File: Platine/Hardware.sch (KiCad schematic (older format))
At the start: 9 parts, among them U1 ESP32-WROOM-32, U2 ZLDO1117_SOT223, U3 TS2596S

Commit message: Spannungsregler hinzugfügt
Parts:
- added C3, C5: 470u, symbol Device:CP
- added C4, C6: 0,1u, symbol Device:C
- added D1: B340A, symbol Device:D_Zener
- added L1: 33u, symbol Device:L
- BT1: renamed from BT?; value Battery -> 9V
- U2: symbol Bauteile_DL7MLP:ZLDO1117_SOT223 -> Hardware-rescue:ZLDO1117_SOT223-Bauteile_DL7MLP
- U3: symbol Bauteile_DL7MLP:TS2596S -> Hardware-rescue:TS2596S-Bauteile_DL7MLP
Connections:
- wire segments 20 -> 50
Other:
- moved on the sheet: BT1

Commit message: Elkos ausgewählt
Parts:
- C3, C5: footprint (none) -> Capacitor_SMD:CP_Elec_6.3x7.7
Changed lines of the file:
@@
 F 0 "C3" H 6318 1146 50  0000 L CNN
 F 1 "470u" H 6318 1055 50  0000 L CNN
-F 2 "" H 6238 950 50  0001 C CNN
-F 3 "~" H 6200 1100 50  0001 C CNN
+F 2 "Capacitor_SMD:CP_Elec_6.3x7.7" H 6238 950 50  0001 C CNN
+F 3 "https://cdn-reichelt.de/documents/datenblatt/B300/SMD_FT_ENG_TDS.pdf" H 6200 1100 50  0001 C CNN
 	1    6200 1100
 	1    0    0    -1
@@
 F 0 "C5" H 8918 1146 50  0000 L CNN
 F 1 "470u" H 8918 1055 50  0000 L CNN
-F 2 "" H 8838 950 50  0001 C CNN
-F 3 "~" H 8800 1100 50  0001 C CNN
+F 2 "Capacitor_SMD:CP_Elec_6.3x7.7" H 8838 950 50  0001 C CNN
+F 3 "reichelt.de/documents/datenblatt/B300/SMD_FT_ENG_TDS.pdf" H 8800 1100 50  0001 C CNN
 	1    8800 1100
 	1    0    0    -1

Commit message: Erweiterung der Bauteilinformationen
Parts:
- removed D1: B340A, symbol Device:D_Zener
- added D1: B340A, symbol Device:D_Schottky
- C4, C6: footprint (none) -> Capacitor_SMD:C_0805_2012Metric_Pad1.18x1.45mm_HandSolder
- L1: footprint (none) -> Inductor_SMD:L_1008_2520Metric_Pad1.43x2.20mm_HandSolder
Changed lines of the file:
@@
 F 0 "C4" H 6615 1146 50  0000 L CNN
 F 1 "0,1u" H 6615 1055 50  0000 L CNN
-F 2 "" H 6538 950 50  0001 C CNN
-F 3 "~" H 6500 1100 50  0001 C CNN
+F 2 "Capacitor_SMD:C_0805_2012Metric_Pad1.18x1.45mm_HandSolder" H 6538 950 50  0001 C CNN
+F 3 "https://cdn-reichelt.de/documents/datenblatt/B300/KEM_C0XXX_C0G_DB-EN.pdf" H 6500 1100 50  0001 C CNN
 	1    6500 1100
 	1    0    0    -1
@@
 F 0 "L1" V 8590 950 50  0000 C CNN
 F 1 "33u" V 8499 950 50  0000 C CNN
-F 2 "" H 8400 950 50  0001 C CNN
-F 3 "~" H 8400 950 50  0001 C CNN
+F 2 "Inductor_SMD:L_1008_2520Metric_Pad1.43x2.20mm_HandSolder" H 8400 950 50  0001 C CNN
+F 3 "https://cdn-reichelt.de/documents/datenblatt/B400/1008F.pdf" H 8400 950 50  0001 C CNN
 	1    8400 950
 	0    -1   -1   0
@@
 F 0 "C6" H 9215 1146 50  0000 L CNN
 F 1 "0,1u" H 9215 1055 50  0000 L CNN
-F 2 "" H 9138 950 50  0001 C CNN
-F 3 "~" H 9100 1100 50  0001 C CNN
+F 2 "Capacitor_SMD:C_0805_2012Metric_Pad1.18x1.45mm_HandSolder" H 9138 950 50  0001 C CNN
+F 3 "https://cdn-reichelt.de/documents/datenblatt/B300/KEM_C0XXX_C0G_DB-EN.pdf" H 9100 1100 50  0001 C CNN
 	1    9100 1100
 	1    0    0    -1
@@
 $EndComp
 $Comp
-L Device:D_Zener D1
-U 1 1 5FB55D4C
-P 8200 1250
-F 0 "D1" V 8154 1330 50  0000 L CNN
-F 1 "B340A" V 8245 1330 50  0000 L CNN
-F 2 "" H 8200 1250 50  0001 C CNN
-F 3 "~" H 8200 1250 50  0001 C CNN
-	1    8200 1250
-	0    1    1    0
-$EndComp
-$Comp
 L power:GND #PWR?
 U 1 1 5FB57356
@@
 Wire Notes Line
 	5450 650  5450 1650
+$Comp
+L Device:D_Schottky D1
+U 1 1 5FB4F340
+P 8200 1250
+F 0 "D1" V 8154 1330 50  0000 L CNN
+F 1 "B340A" V 8245 1330 50  0000 L CNN
+F 2 "" H 8200 1250 50  0001 C CNN
+F 3 "~" H 8200 1250 50  0001 C CNN
+	1    8200 1250
+	0    1    1    0
+$EndComp
 $EndSCHEMATC

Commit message: Finished LED Matrix Added part datasheets Updated BOM
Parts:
- removed C? (x2): C, symbol Device:C
- removed U1: ESP32-WROOM-32, RF_Module:ESP32-WROOM-32, symbol RF_Module:ESP32-WROOM-32
- added C?: 100n, Resistor_SMD:R_0805_2012Metric_Pad1.15x1.40mm_HandSolder, symbol Device:C
- added C? (x41): 100n, symbol Device:C
- added D? (x41): WS2812S, LED_SMD:LED_WS2812_PLCC6_5.0x5.0mm_P1.6mm, symbol LED:WS2812S
- added R? (x42): 91, Resistor_SMD:R_0805_2012Metric_Pad1.15x1.40mm_HandSolder, symbol Device:R
- added U1: ESP32-WROOM-32D, RF_Module:ESP32-WROOM-32, symbol RF_Module:ESP32-WROOM-32D
- D1: footprint (none) -> Diode_SMD:D_SMA_Handsoldering
- L1: footprint Inductor_SMD:L_1008_2520Metric_Pad1.43x2.20mm_HandSolder -> Footprints_DL7MLP:L_1008_2520Metric_Pad1.43x2.20mm_HandSolder
- U2: symbol Hardware-rescue:ZLDO1117_SOT223-Bauteile_DL7MLP -> Bauteile_DL7MLP:ZLDO1117_SOT223
- U3: symbol Hardware-rescue:TS2596S-Bauteile_DL7MLP -> Bauteile_DL7MLP:TS2596S
- gave numbers to parts that had none: 1
- renumbered D1 to D2
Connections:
- wire segments 50 -> 556
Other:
- note added: "Led Matrix\nSpielfeld"
- note added: "Regulator 3V3"
- note added: "Regulator 5V"
- moved on the sheet: BT1, C1, C2, C3, C4, C5, C6, D1, D2, L1

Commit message: LED-Matrix Baueilnummerierung hinzugefügt und BOM erweitert
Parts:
- C10, C11, C12, C13, C14, C15, C16, C17, C18, C19, C20, C21, C22, C23, C24, C25, C26, C27, C28, C29, C30, C31, C32, C33, C34, C35, C36, C37, C38, C39, C40, C41, C42, C43, C44, C45, C46, C47, C48, C8, C9: renamed from C?; footprint (none) -> Resistor_SMD:R_0805_2012Metric_Pad1.15x1.40mm_HandSolder
- L1: footprint Footprints_DL7MLP:L_1008_2520Metric_Pad1.43x2.20mm_HandSolder -> Custom_Footprints:L_1008_2520Metric_Pad1.43x2.20mm_HandSolder
- U2: symbol Bauteile_DL7MLP:ZLDO1117_SOT223 -> Custom_Symbols:ZLDO1117_SOT223
- U3: symbol Bauteile_DL7MLP:TS2596S -> Custom_Symbols:TS2596S
- gave numbers to parts that had none: 84

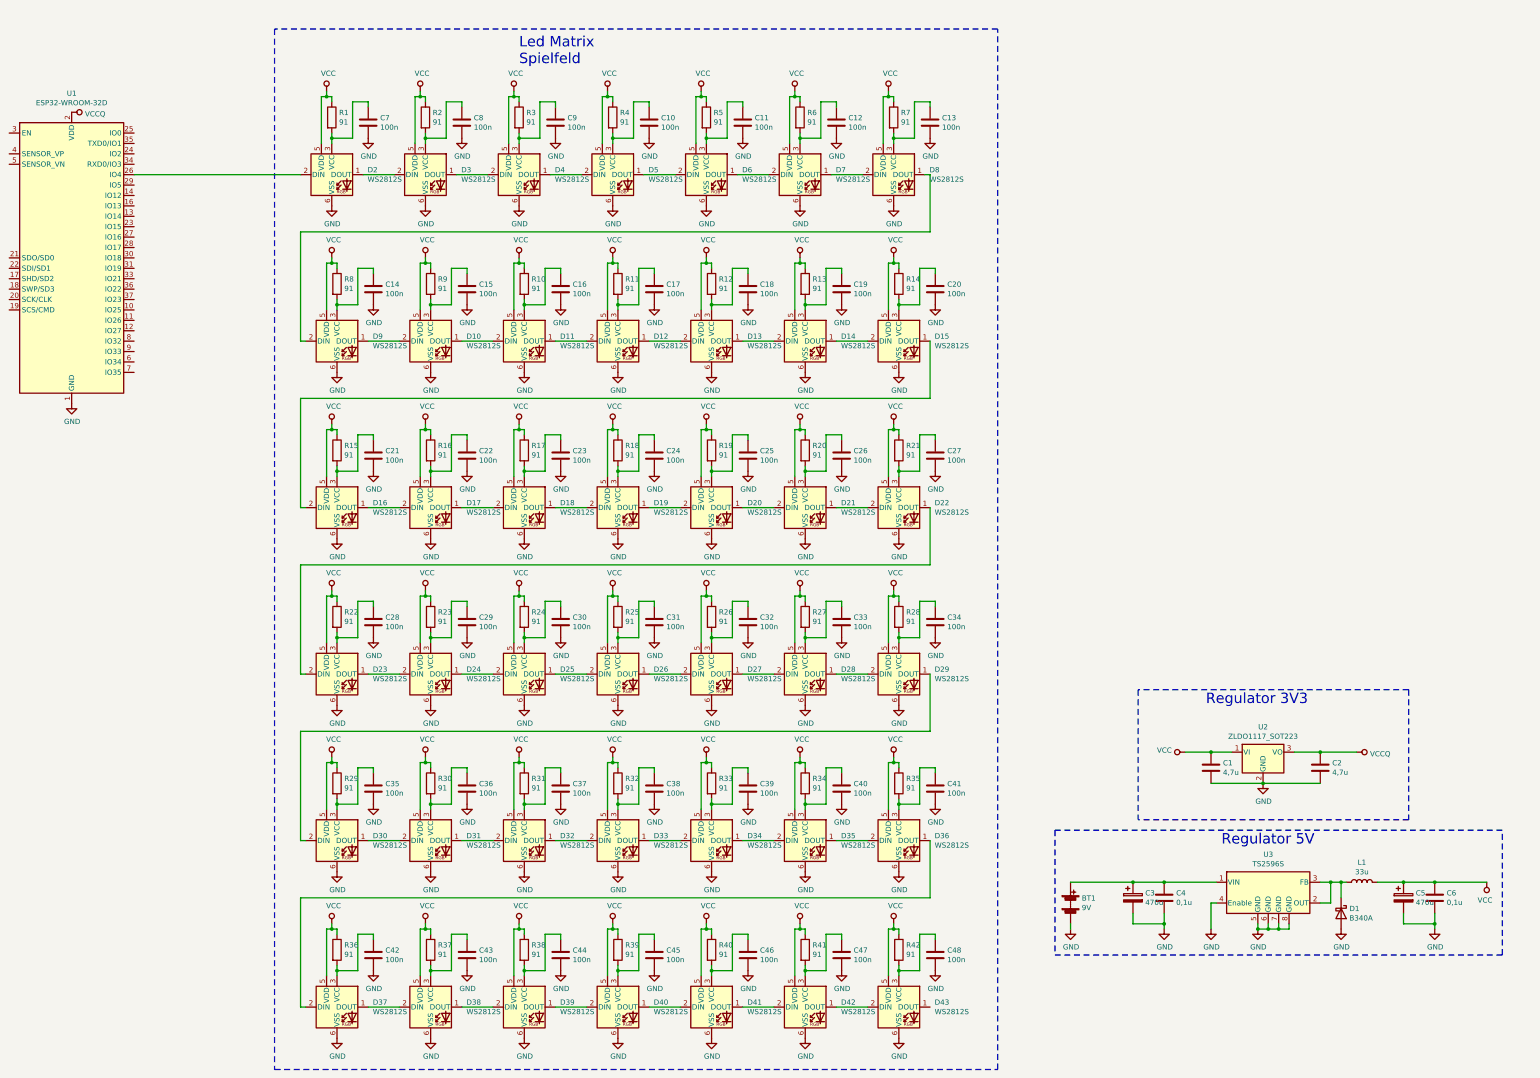
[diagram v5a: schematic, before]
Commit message: Added LED matrix spaceing Added Soft-Reset Added Hard-Reset Added USB-Interface Added Programming-Button Added ISP-Programmer Created 3D Frontplate mockup
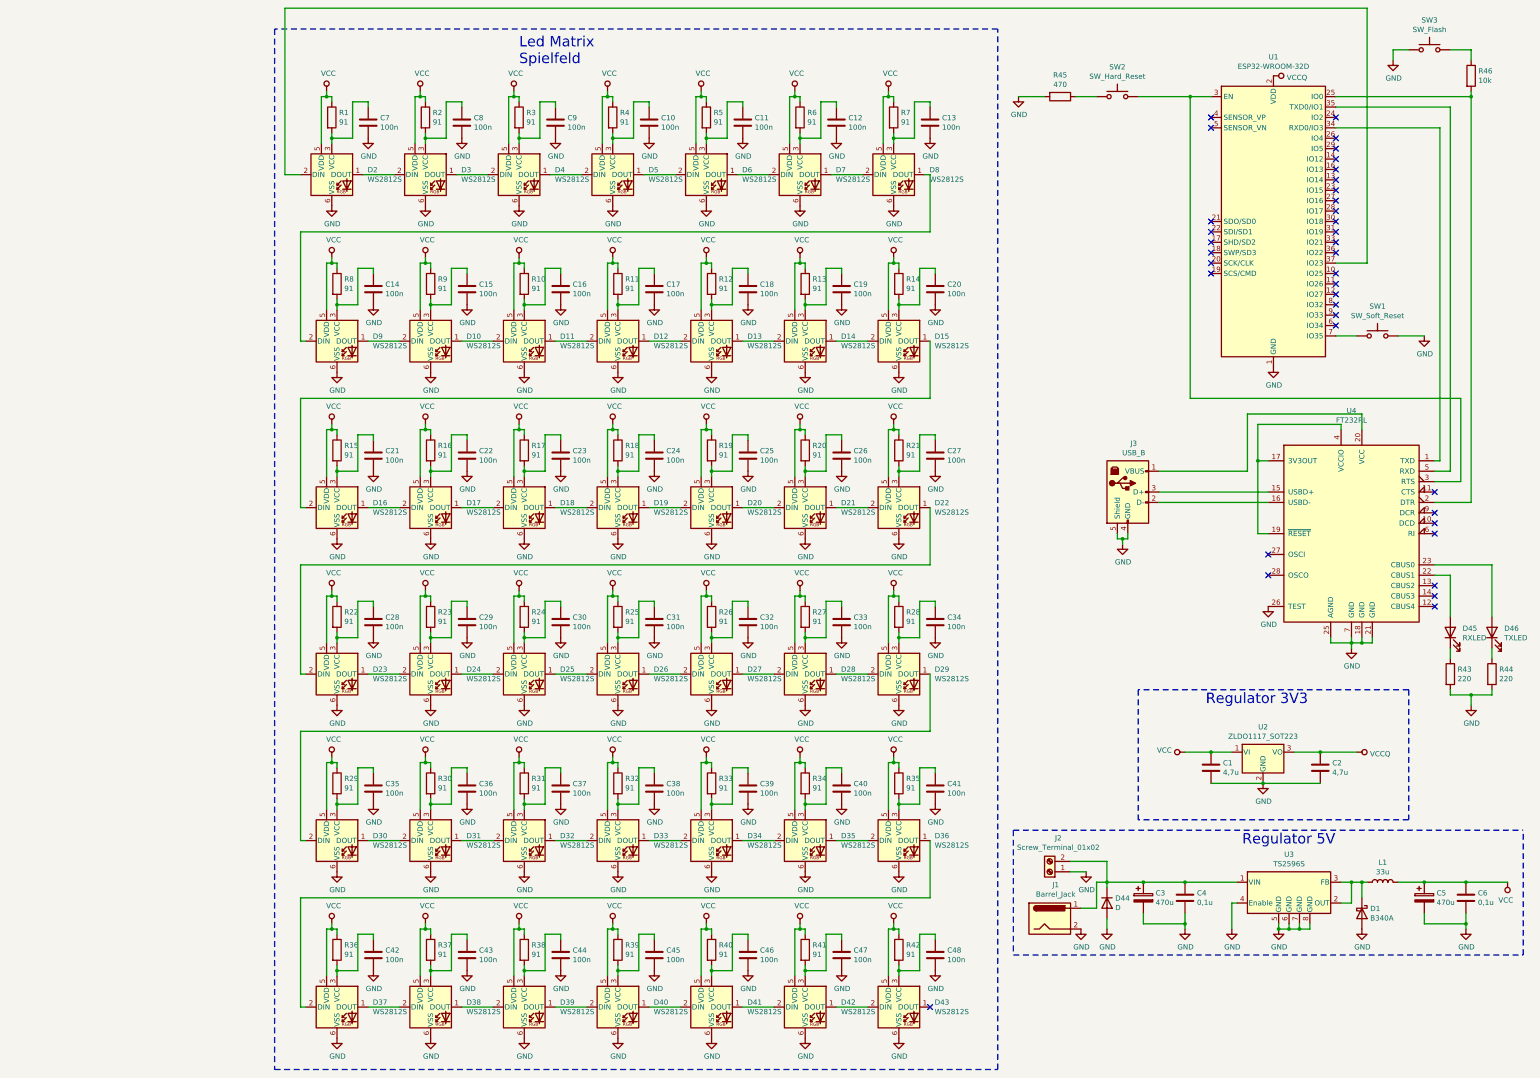
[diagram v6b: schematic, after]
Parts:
- removed BT1: 9V, symbol Device:Battery
- added D44: D, Diode_SMD:D_SMA_Handsoldering, symbol Device:D
- added D45: RXLED, LED_SMD:LED_0805_2012Metric_Pad1.15x1.40mm_HandSolder, symbol Device:LED
- added D46: TXLED, LED_SMD:LED_0805_2012Metric_Pad1.15x1.40mm_HandSolder, symbol Device:LED
- added J1: Barrel_Jack, Connector_BarrelJack:BarrelJack_Horizontal, symbol Connector:Barrel_Jack
- added J2: Screw_Terminal_01x02, TerminalBlock_RND:TerminalBlock_RND_205-00001_1x02_P5.00mm_Horizontal, symbol Connector:Screw_Terminal_01x02
- added J3: USB_B, Connector_USB:USB_B_OST_USB-B1HSxx_Horizontal, symbol Connector:USB_B
- added R43, R44: 220, Resistor_SMD:R_0805_2012Metric_Pad1.15x1.40mm_HandSolder, symbol Device:R
- added R45: 470, Resistor_SMD:R_0805_2012Metric_Pad1.15x1.40mm_HandSolder, symbol Device:R
- added R46: 10k, Resistor_SMD:R_0805_2012Metric_Pad1.15x1.40mm_HandSolder, symbol Device:R
- added SW1: SW_Soft_Reset, Custom_Footprints:SW_1612.11, symbol Switch:SW_Push
- added SW2: SW_Hard_Reset, Custom_Footprints:SW_1612.11, symbol Switch:SW_Push
- added SW3: SW_Flash, Custom_Footprints:SW_1612.11, symbol Switch:SW_Push
- added U4: FT232RL, Package_SO:SSOP-28_5.3x10.2mm_P0.65mm, symbol Interface_USB:FT232RL
- C4, C6: footprint Capacitor_SMD:C_0805_2012Metric_Pad1.18x1.45mm_HandSolder -> Capacitor_SMD:C_0805_2012Metric_Pad1.15x1.40mm_HandSolder
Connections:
- net GND: now also D44.2 (A), J1.2, J2.1 (Pin_1), J3.4 (GND), J3.5 (Shield), R43.2, R44.2, R45.2, SW1.2, SW3.1, U4.18 (GND), U4.21 (GND), U4.25 (AGND), U4.26 (TEST), U4.7 (GND)
- net at C3.1, C4.1, U3.1 (VIN): now also D44.1 (K), J1.1, J2.2 (Pin_2)
- net at U1.25 (IO0): now also R46.2, U4.2 (DTR)
- net at U1.26 (IO4): no longer D2.2 (DIN)
- net at U1.3 (EN): now also SW2.2, U4.3 (RTS)
- net at U1.34 (RXD0/IO3): now also U4.1 (TXD)
- net at U1.35 (TXD0/IO1): now also U4.5 (RXD)
- net at U1.37 (IO23): now also D2.2 (DIN)
- net at U1.7 (IO35): now also SW1.1
- new net: J3.3 (D+), U4.15 (USBD+)
- new net: J3.2 (D-), U4.16 (USBD-)
- new net: U4.17 (3V3OUT), U4.19 (~RESET~), U4.4 (VCCIO)
- new net: J3.1 (VBUS), U4.20 (VCC)
- new net: D45.2 (A), U4.22 (CBUS1)
- new net: D46.2 (A), U4.23 (CBUS0)
- new net: R45.1, SW2.1
- new net: D45.1 (K), R43.1
- new net: D46.1 (K), R44.1
- new net: R46.1, SW3.2
- no-connect marks 0 -> 37
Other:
- moved on the sheet: C3, C4, C5, C6, D1, L1, U1, U3

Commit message: Updated Schematic to be more intuitive to read Updated BOM
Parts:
- added C49, C50: 100n, symbol Device:C
- added C51: 4.7u, symbol Device:C
- added Q1, Q2: BCX19, Package_TO_SOT_SMD:SOT-23, symbol Custom_Symbols:BCX19
- added R47, R48: 10k, symbol Device:R
- R45: value 470 -> 10k; footprint Resistor_SMD:R_0805_2012Metric_Pad1.15x1.40mm_HandSolder -> (none)
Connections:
- net GND: now also SW1.1, SW2.1, C49.2, C50.2, C51.2; no longer R45.2, SW1.2
- net VCCQ: now also R45.1, R46.1
- net ESP_ENA: now reaches SW2.2, U1.3 (EN)
- net ESP_ENA: now also R45.2, Q1.2 (C); no longer U4.3 (RTS)
- net RX0: now reaches U4.1 (TXD)
- net RX0: now also U1.35 (TXD0/IO1); no longer U1.34 (RXD0/IO3)
- net TX0: now reaches U4.5 (RXD)
- net TX0: now also U1.34 (RXD0/IO3); no longer U1.35 (TXD0/IO1)
- net LED_DATA: now reaches D2.2 (DIN), U1.37 (IO23)
- net IO_S_RST: now reaches U1.7 (IO35)
- net IO_S_RST: now also SW1.2; no longer SW1.1
- net V_FT_IO: now reaches U4.17 (3V3OUT), U4.19 (~RESET~), U4.4 (VCCIO)
- net V_FT_IO: now also C50.1
- net V_USB: now reaches J3.1 (VBUS), U4.20 (VCC)
- net V_USB: now also C49.1, C51.1
- net GPIO_0: now reaches SW3.2
- net GPIO_0: now also R46.2, Q2.2 (C); no longer R46.1
- new net: Q1.1 (B), R47.1
- new net: Q2.1 (B), R48.1
- new net DTR: Q2.3 (E), R47.2, U4.2 (DTR)
- new net RTS: Q1.3 (E), R48.2, U4.3 (RTS)
- now unconnected: U1.25 (IO0)
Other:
- note added: "Button Boot"
- note added: "Button Reset"
- note added: "Button Soft Reset"
- note added: "MCU ESP32 WROOM 32D"
- note added: "Reset Logic"
- note added: "USB / UART Wandler"
- moved on the sheet: C1, C10, C11, C12, C13, C14, C15, C16, C17, C18, C19, C2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

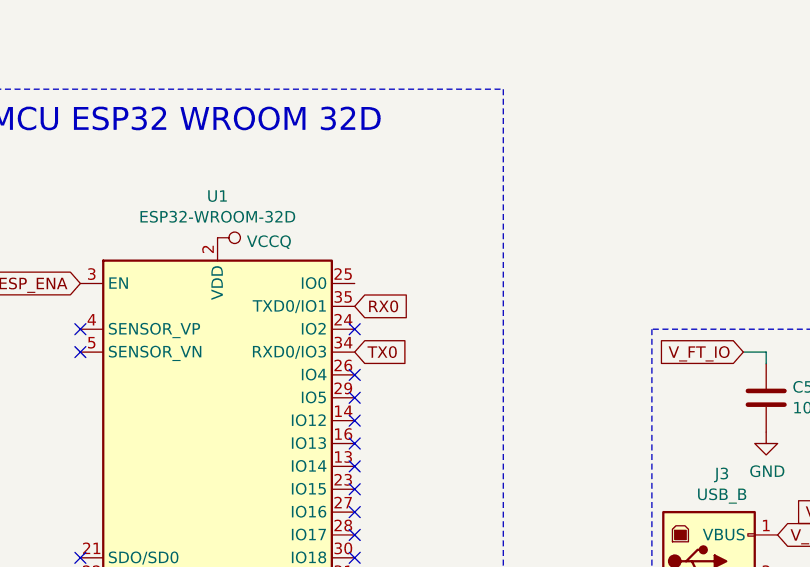
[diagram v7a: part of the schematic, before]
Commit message: Added Enclosure plan
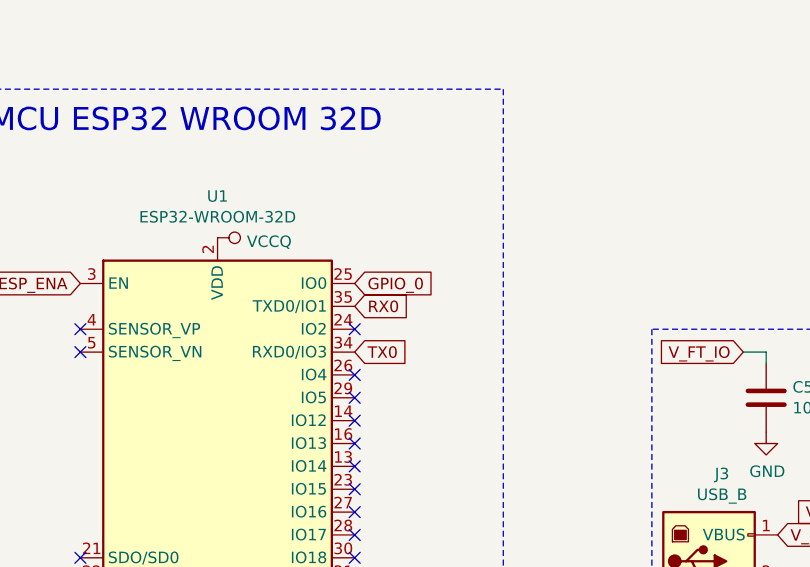
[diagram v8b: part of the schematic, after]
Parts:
- C49, C50, C51: footprint (none) -> Capacitor_SMD:C_0805_2012Metric_Pad1.15x1.40mm_HandSolder
- R45, R47, R48: footprint (none) -> Resistor_SMD:R_0805_2012Metric_Pad1.15x1.40mm_HandSolder
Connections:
- net GPIO_0: now also U1.25 (IO0)
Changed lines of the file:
@@
 EESchema Schematic File Version 4
+LIBS:Hardware-cache
 EELAYER 30 0
 EELAYER END
@@
 F 0 "R47" V 9593 8950 50  0000 C CNN
 F 1 "10k" V 9684 8950 50  0000 C CNN
-F 2 "" V 9730 8950 50  0001 C CNN
+F 2 "Resistor_SMD:R_0805_2012Metric_Pad1.15x1.40mm_HandSolder" V 9730 8950 50  0001 C CNN
 F 3 "~" H 9800 8950 50  0001 C CNN
 	1    9800 8950
@@
 F 0 "R48" V 9593 9550 50  0000 C CNN
 F 1 "10k" V 9684 9550 50  0000 C CNN
-F 2 "" V 9730 9550 50  0001 C CNN
+F 2 "Resistor_SMD:R_0805_2012Metric_Pad1.15x1.40mm_HandSolder" V 9730 9550 50  0001 C CNN
 F 3 "~" H 9800 9550 50  0001 C CNN
 	1    9800 9550
@@
 $EndComp
 $Comp
-L power:VCCQ #PWR?
+L power:VCCQ #PWR0248
 U 1 1 62296A35
 P 8550 9250
-F 0 "#PWR?" H 8550 9100 50  0001 C CNN
+F 0 "#PWR0248" H 8550 9100 50  0001 C CNN
 F 1 "VCCQ" H 8567 9423 50  0000 C CNN
 F 2 "" H 8550 9250 50  0001 C CNN
@@
 F 0 "R45" H 8620 9496 50  0000 L CNN
 F 1 "10k" H 8620 9405 50  0000 L CNN
-F 2 "" V 8480 9450 50  0001 C CNN
+F 2 "Resistor_SMD:R_0805_2012Metric_Pad1.15x1.40mm_HandSolder" V 8480 9450 50  0001 C CNN
 F 3 "~" H 8550 9450 50  0001 C CNN
 	1    8550 9450
@@
 	8550 10850 8550 10900
 $Comp
-L power:VCCQ #PWR?
+L power:VCCQ #PWR0249
 U 1 1 62A1849F
 P 8550 10500
-F 0 "#PWR?" H 8550 10350 50  0001 C CNN
+F 0 "#PWR0249" H 8550 10350 50  0001 C CNN
 F 1 "VCCQ" H 8567 10673 50  0000 C CNN
 F 2 "" H 8550 10500 50  0001 C CNN
@@
 F 0 "C49" H 12665 8246 50  0000 L CNN
 F 1 "100n" H 12665 8155 50  0000 L CNN
-F 2 "" H 12588 8050 50  0001 C CNN
+F 2 "Capacitor_SMD:C_0805_2012Metric_Pad1.15x1.40mm_HandSolder" H 12588 8050 50  0001 C CNN
 F 3 "~" H 12550 8200 50  0001 C CNN
 	1    12550 8200
@@
 F 0 "C51" H 13065 8246 50  0000 L CNN
 F 1 "4.7u" H 13065 8155 50  0000 L CNN
-F 2 "" H 12988 8050 50  0001 C CNN
+F 2 "Capacitor_SMD:C_0805_2012Metric_Pad1.15x1.40mm_HandSolder" H 12988 8050 50  0001 C CNN
 F 3 "~" H 12950 8200 50  0001 C CNN
 	1    12950 8200
@@
 	12950 8400 12950 8350
 $Comp
-L power:GND #PWR?
+L power:GND #PWR0250
 U 1 1 63DBF9ED
 P 12750 8400
-F 0 "#PWR?" H 12750 8150 50  0001 C CNN
+F 0 "#PWR0250" H 12750 8150 50  0001 C CNN
 F 1 "GND" H 12755 8227 50  0000 C CNN
 F 2 "" H 12750 8400 50  0001 C CNN
@@
 F 0 "C50" H 13015 5896 50  0000 L CNN
 F 1 "100n" H 13015 5805 50  0000 L CNN
-F 2 "" H 12938 5700 50  0001 C CNN
+F 2 "Capacitor_SMD:C_0805_2012Metric_Pad1.15x1.40mm_HandSolder" H 12938 5700 50  0001 C CNN
 F 3 "~" H 12900 5850 50  0001 C CNN
 	1    12900 5850
@@
 	12900 5650 12900 5700
 $Comp
-L power:GND #PWR?
+L power:GND #PWR0251
 U 1 1 641DD522
 P 12900 6000
-F 0 "#PWR?" H 12900 5750 50  0001 C CNN
+F 0 "#PWR0251" H 12900 5750 50  0001 C CNN
 F 1 "GND" H 12905 5827 50  0000 C CNN
 F 2 "" H 12900 6000 50  0001 C CNN
@@
 Text Notes 9500 4700 0    100  ~ 0
 MCU ESP32 WROOM 32D
+Text GLabel 11100 5350 2    50   Input ~ 0
+GPIO_0
 $EndSCHEMATC
